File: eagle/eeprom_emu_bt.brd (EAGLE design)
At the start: 100 x 80 mm, 9 parts

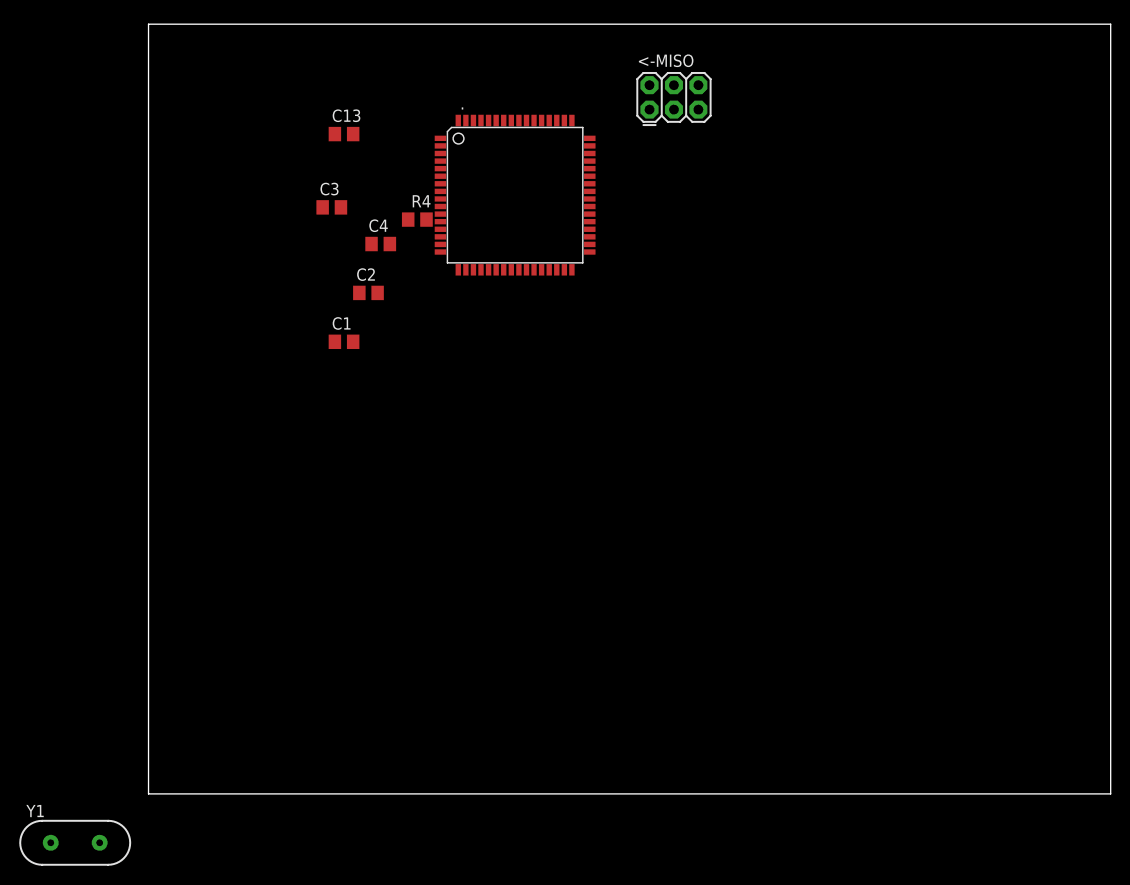
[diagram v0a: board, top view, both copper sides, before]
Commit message: 27c256 added
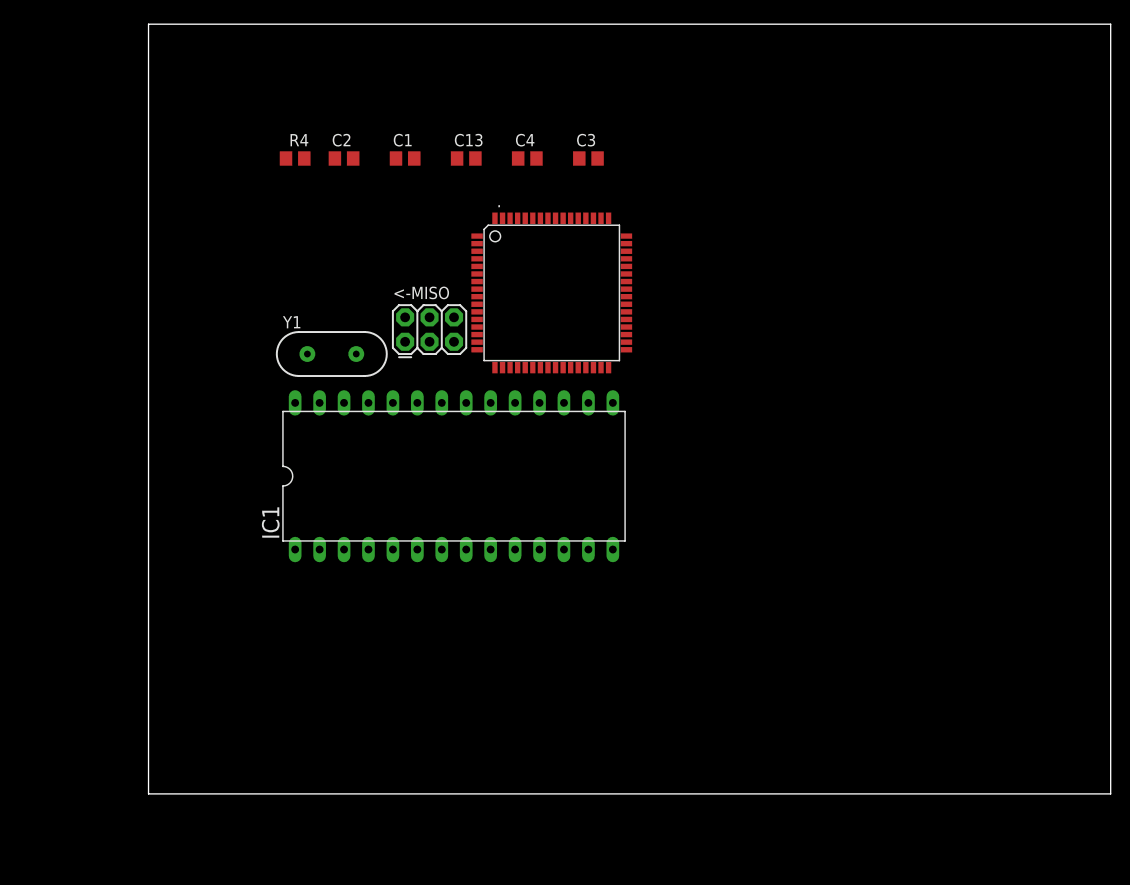
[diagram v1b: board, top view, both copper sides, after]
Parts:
- added IC1: (no value), memory:DIL28
- moved Y1 57.4 mm to (19.1, 45.7)
- moved <-MISO 35.0 mm to (26.7, 47.0)
- moved C3 27.1 mm to (45.7, 66.0)
- moved C1 20.1 mm to (26.7, 66.0)
- moved C4 17.6 mm to (39.4, 66.0)
- moved C2 14.2 mm to (20.3, 66.0)
- moved R4 14.2 mm to (15.2, 66.0)
- moved C13 13.0 mm to (33.0, 66.0)
- moved . 10.9 mm to (41.9, 52.1)
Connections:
- net GND: now also IC1.14
- net VCC: now also IC1.28
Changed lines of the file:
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@@
 </autorouter>
 <elements>
-<element name="." library="avr-7" package="TQFP64" value="MEGA128-A" x="38.1" y="62.23"/>
-<element name="&lt;-MISO" library="SparkFun-Connectors" package="2X3" value="ICSP" x="52.07" y="71.12"/>
-<element name="C1" library="resistor" package="C0805" value="22pF" x="20.32" y="46.99"/>
-<element name="C13" library="resistor" package="C0805" value="100nF" x="20.32" y="68.58"/>
-<element name="C2" library="resistor" package="C0805" value="22pF" x="22.86" y="52.07"/>
-<element name="C3" library="resistor" package="C0805" value="100nF" x="19.05" y="60.96"/>
-<element name="C4" library="resistor" package="C0805" value="100nF" x="24.13" y="57.15"/>
-<element name="R4" library="rcl" package="R0805" value="5k" x="27.94" y="59.69"/>
-<element name="Y1" library="SparkFun-FreqCtrl" package="HC49US" value="" x="-7.62" y="-5.08"/>
+<element name="." library="avr-7" package="TQFP64" value="MEGA128-A" x="41.91" y="52.07"/>
+<element name="&lt;-MISO" library="SparkFun-Connectors" package="2X3" value="ICSP" x="26.67" y="46.99"/>
+<element name="C1" library="resistor" package="C0805" value="22pF" x="26.67" y="66.04"/>
+<element name="C13" library="resistor" package="C0805" value="100nF" x="33.02" y="66.04"/>
+<element name="C2" library="resistor" package="C0805" value="22pF" x="20.32" y="66.04"/>
+<element name="C3" library="resistor" package="C0805" value="100nF" x="45.72" y="66.04"/>
+<element name="C4" library="resistor" package="C0805" value="100nF" x="39.37" y="66.04"/>
+<element name="IC1" library="memory" package="DIL28" value="" x="31.75" y="33.02"/>
+<element name="R4" library="rcl" package="R0805" value="5k" x="15.24" y="66.04"/>
+<element name="Y1" library="SparkFun-FreqCtrl" package="HC49US" value="" x="19.05" y="45.72"/>
 </elements>
 <signals>
-<signal name="N$1">
-<contactref element="." pad="24"/>
-<contactref element="C2" pad="2"/>
-<contactref element="Y1" pad="1"/>
-<wire x1="23.81" y1="52.07" x2="37.7063" y2="54.4703" width="0" layer="19" extent="1-1"/>
-<wire x1="-10.16" y1="-5.08" x2="23.81" y2="52.07" width="0" layer="19" extent="1-1"/>
-</signal>
-<signal name="N$2">
-<contactref element="." pad="23"/>
-<contactref element="C1" pad="2"/>
-<contactref element="Y1" pad="2"/>
-<wire x1="21.27" y1="46.99" x2="36.9189" y2="54.4703" width="0" layer="19" extent="1-1"/>
-<wire x1="-5.08" y1="-5.08" x2="21.27" y2="46.99" width="0" layer="19" extent="1-1"/>
-</signal>
 <signal name="GND">
+<contactref element="IC1" pad="14"/>
 <contactref element="C2" pad="1"/>
 <contactref element="C1" pad="1"/>
@@
 <contactref element="&lt;-MISO" pad="6"/>
 <contactref element="C13" pad="2"/>
-<wire x1="36.1315" y1="54.4703" x2="57.15" y2="73.66" width="0" layer="19" extent="1-1"/>
-<wire x1="32.9819" y1="69.9897" x2="57.15" y2="73.66" width="0" layer="19" extent="1-1"/>
-<wire x1="40.8559" y1="69.9897" x2="32.9819" y2="69.9897" width="0" layer="19" extent="1-1"/>
-<wire x1="20" y1="60.96" x2="32.9819" y2="69.9897" width="0" layer="19" extent="1-1"/>
-<wire x1="25.08" y1="57.15" x2="20" y2="60.96" width="0" layer="19" extent="1-1"/>
-<wire x1="21.91" y1="52.07" x2="20" y2="60.96" width="0" layer="19" extent="1-1"/>
-<wire x1="19.37" y1="46.99" x2="21.91" y2="52.07" width="0" layer="19" extent="1-1"/>
-<wire x1="21.27" y1="68.58" x2="19.37" y2="46.99" width="0" layer="19" extent="1-1"/>
+<wire x1="40.32" y1="66.04" x2="46.67" y2="66.04" width="0" layer="19" extent="1-1"/>
+<wire x1="33.97" y1="66.04" x2="40.32" y2="66.04" width="0" layer="19" extent="1-1"/>
+<wire x1="44.6659" y1="59.8297" x2="46.67" y2="66.04" width="0" layer="19" extent="1-1"/>
+<wire x1="36.7919" y1="59.8297" x2="33.97" y2="66.04" width="0" layer="19" extent="1-1"/>
+<wire x1="25.72" y1="66.04" x2="33.97" y2="66.04" width="0" layer="19" extent="1-1"/>
+<wire x1="19.37" y1="66.04" x2="25.72" y2="66.04" width="0" layer="19" extent="1-1"/>
+<wire x1="31.75" y1="49.53" x2="36.7919" y2="59.8297" width="0" layer="19" extent="1-1"/>
+<wire x1="39.9415" y1="44.3103" x2="31.75" y2="49.53" width="0" layer="19" extent="1-1"/>
+<wire x1="48.26" y1="25.4" x2="39.9415" y2="44.3103" width="0" layer="19" extent="1-1"/>
 </signal>
 <signal name="VCC">
+<contactref element="IC1" pad="28"/>
 <contactref element="." pad="64"/>
 <contactref element="C4" pad="1"/>
@@
 <contactref element="C13" pad="1"/>
 <contactref element="." pad="52"/>
-<wire x1="35.3441" y1="54.4703" x2="52.07" y2="73.66" width="0" layer="19" extent="1-1"/>
-<wire x1="32.1945" y1="69.9897" x2="52.07" y2="73.66" width="0" layer="19" extent="1-1"/>
-<wire x1="18.1" y1="60.96" x2="32.1945" y2="69.9897" width="0" layer="19" extent="1-1"/>
-<wire x1="23.18" y1="57.15" x2="18.1" y2="60.96" width="0" layer="19" extent="1-1"/>
-<wire x1="41.6433" y1="69.9897" x2="32.1945" y2="69.9897" width="0" layer="19" extent="1-1"/>
-<wire x1="28.89" y1="59.69" x2="18.1" y2="60.96" width="0" layer="19" extent="1-1"/>
-<wire x1="19.37" y1="68.58" x2="28.89" y2="59.69" width="0" layer="19" extent="1-1"/>
+<wire x1="26.67" y1="49.53" x2="15.24" y2="40.64" width="0" layer="19" extent="1-1"/>
+<wire x1="39.1541" y1="44.3103" x2="26.67" y2="49.53" width="0" layer="19" extent="1-1"/>
+<wire x1="36.0045" y1="59.8297" x2="26.67" y2="49.53" width="0" layer="19" extent="1-1"/>
+<wire x1="38.42" y1="66.04" x2="36.0045" y2="59.8297" width="0" layer="19" extent="1-1"/>
+<wire x1="44.77" y1="66.04" x2="38.42" y2="66.04" width="0" layer="19" extent="1-1"/>
+<wire x1="45.4533" y1="59.8297" x2="44.77" y2="66.04" width="0" layer="19" extent="1-1"/>
+<wire x1="32.07" y1="66.04" x2="38.42" y2="66.04" width="0" layer="19" extent="1-1"/>
+<wire x1="16.19" y1="66.04" x2="32.07" y2="66.04" width="0" layer="19" extent="1-1"/>
+</signal>
+<signal name="N$1">
+<contactref element="." pad="24"/>
+<contactref element="C2" pad="2"/>
+<contactref element="Y1" pad="1"/>
+<wire x1="21.27" y1="66.04" x2="16.51" y2="45.72" width="0" layer="19" extent="1-1"/>
+<wire x1="41.5163" y1="44.3103" x2="16.51" y2="45.72" width="0" layer="19" extent="1-1"/>
+</signal>
+<signal name="N$2">
+<contactref element="." pad="23"/>
+<contactref element="C1" pad="2"/>
+<contactref element="Y1" pad="2"/>
+<wire x1="40.7289" y1="44.3103" x2="21.59" y2="45.72" width="0" layer="19" extent="1-1"/>
+<wire x1="27.62" y1="66.04" x2="21.59" y2="45.72" width="0" layer="19" extent="1-1"/>
 </signal>
 <signal name="A9">
@@
 <contactref element="&lt;-MISO" pad="4"/>
 <contactref element="." pad="2"/>
-<wire x1="30.3403" y1="67.3481" x2="54.61" y2="73.66" width="0" layer="19" extent="1-1"/>
+<wire x1="34.1503" y1="57.1881" x2="29.21" y2="49.53" width="0" layer="19" extent="1-1"/>
 </signal>
 <signal name="MISO">
 <contactref element="&lt;-MISO" pad="1"/>
 <contactref element="." pad="3"/>
-<wire x1="30.3403" y1="66.5607" x2="52.07" y2="71.12" width="0" layer="19" extent="1-1"/>
+<wire x1="34.1503" y1="56.4007" x2="26.67" y2="46.99" width="0" layer="19" extent="1-1"/>
 </signal>
 <signal name="SCK">
 <contactref element="&lt;-MISO" pad="3"/>
 <contactref element="." pad="11"/>
-<wire x1="30.3403" y1="60.2615" x2="54.61" y2="71.12" width="0" layer="19" extent="1-1"/>
+<wire x1="34.1503" y1="50.1015" x2="29.21" y2="46.99" width="0" layer="19" extent="1-1"/>
 </signal>
 <signal name="RESET">
@@
 <contactref element="R4" pad="1"/>
 <contactref element="&lt;-MISO" pad="5"/>
-<wire x1="34.5567" y1="54.4703" x2="57.15" y2="71.12" width="0" layer="19" extent="1-1"/>
-<wire x1="26.99" y1="59.69" x2="57.15" y2="71.12" width="0" layer="19" extent="1-1"/>
+<wire x1="38.3667" y1="44.3103" x2="31.75" y2="46.99" width="0" layer="19" extent="1-1"/>
+<wire x1="14.29" y1="66.04" x2="31.75" y2="46.99" width="0" layer="19" extent="1-1"/>
 </signal>
 </signals>

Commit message: eagles
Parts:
- added BLUETOOTH: (no value), SparkFun-Connectors:1X05
- added IC2: IS62C256AL-45U, memory-issi-asynsram:SOP28-330MIL
- added IC3, IC4, IC5, IC6, IC7, IC8: 74HCT541DW, 74xx-eu:SO20W
- added IC9: 74HC573D, 74xx-eu:SO20W
- added U1: SST39SF040-70-4I-NHE, Silicon_Storage_Tech_By_element14_Batch_1:PLCC127P1244X1498X357-32N
- moved C3 38.4 mm to (7.62, 61.0)
- moved IC1 34.3 mm to (53.3, 59.7), turned to 270 degrees
- moved C2 27.7 mm to (12.7, 39.4)
- moved C1 27.4 mm to (20.3, 39.4)
- moved . 24.2 mm to (17.8, 50.8)
- moved <-MISO 21.7 mm to (6.35, 39.4), turned to 90 degrees
- moved C4 17.3 mm to (22.9, 61.0)
- moved C13 16.1 mm to (17.8, 61.0)
- moved Y1 10.9 mm to (15.2, 35.6)
- moved R4 5.68 mm to (12.7, 61.0)
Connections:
- new net VDD: IC2.28, U1.32
- net GND: now also IC2.14, IC3.10, IC4.10, IC5.10, IC6.10, IC7.10, IC8.10, IC9.10
- net VCC: now also IC3.20, IC4.20, IC5.20, IC6.20, IC7.20, IC8.20, IC9.20
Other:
- board size 100 x 80 mm -> 64.4 x 47 mm
